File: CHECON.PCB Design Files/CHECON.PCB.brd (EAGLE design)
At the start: 81.7 x 51.7 mm, 48 parts

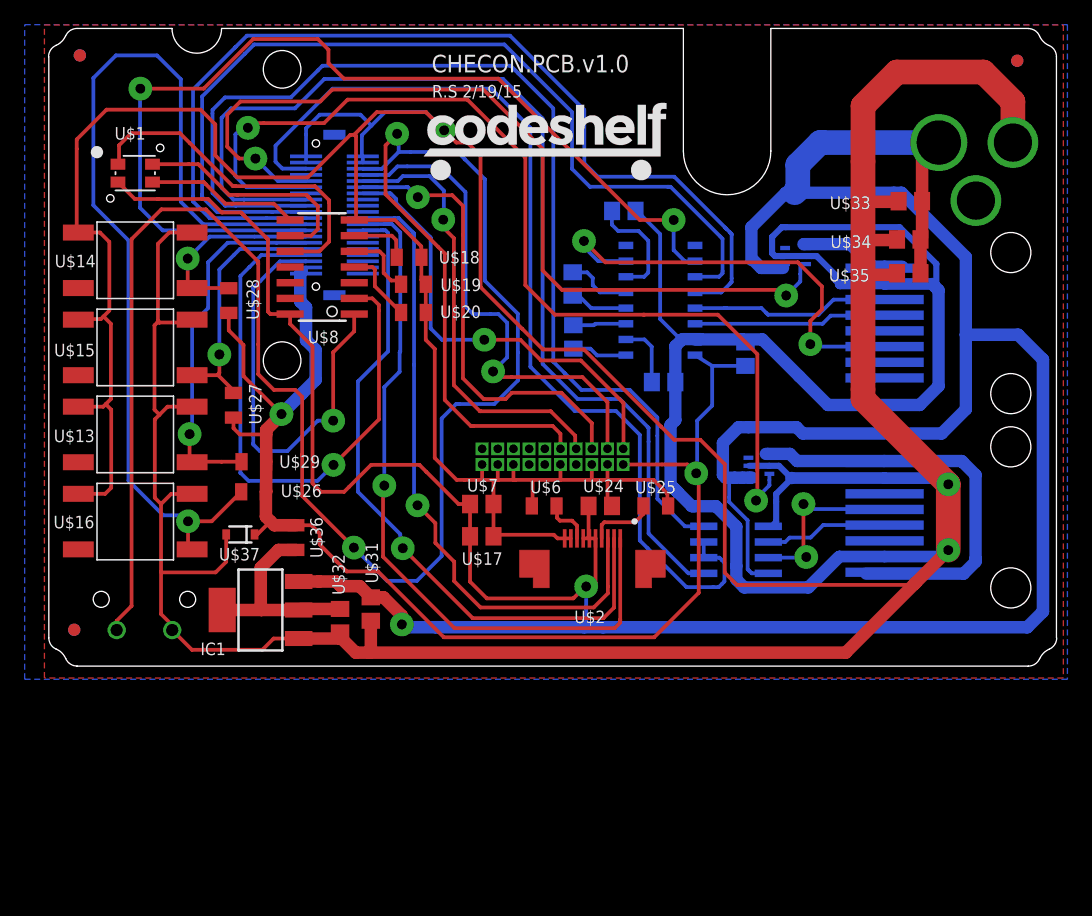
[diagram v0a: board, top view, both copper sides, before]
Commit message: CHECON.PCB.V1.0
Fixed some pin 1 markers, grounded unused input on 232, package names,
flipped FPC pins to correct pin 1 location
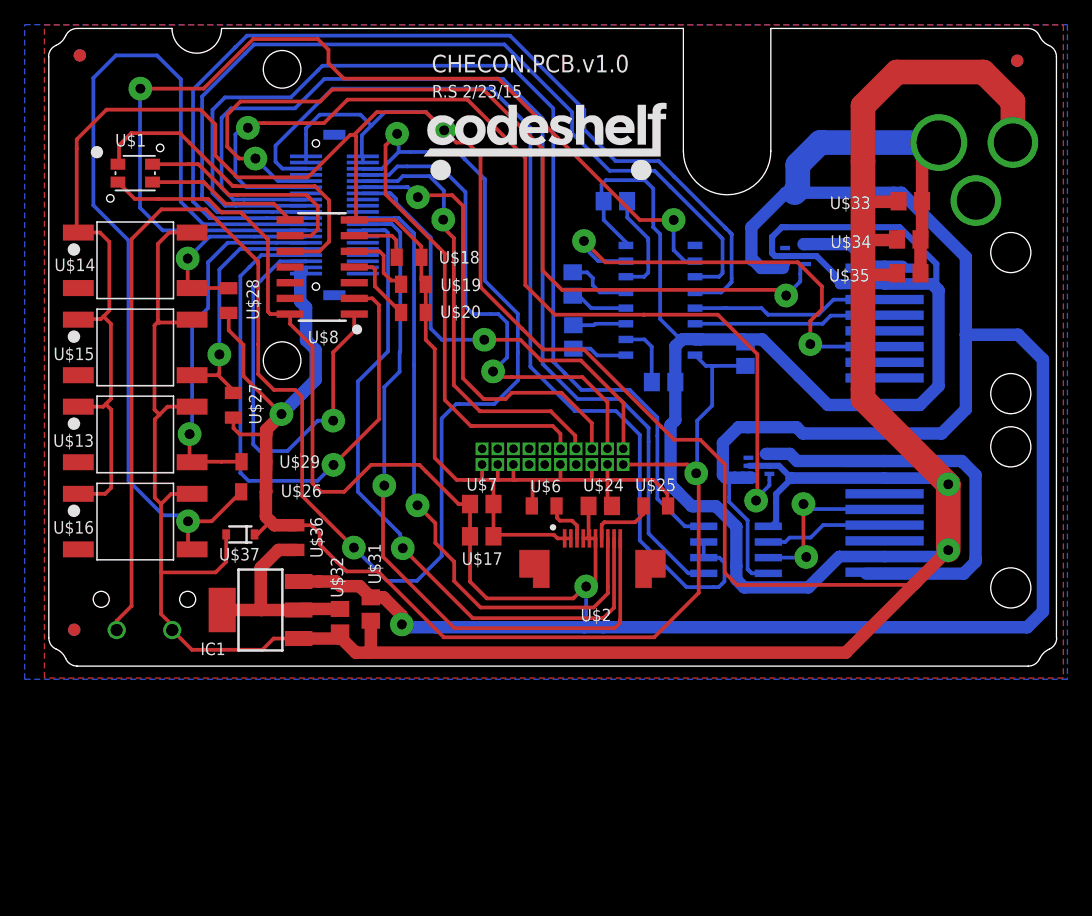
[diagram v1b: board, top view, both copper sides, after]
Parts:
- POSCON, SCANNER: device GW-devices:MOLEX-0955016649 -> GW-devices:RJ45_SMD
- U$1: device KW2:RGBLED -> KW2:PLCC4_SMALL
- U$2: device KW2:52745-1097 -> KW2:FPC
- moved U$23 1.04 mm to (5.08, 11.8), turned to 0 degrees
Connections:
- net GND: now also U$2.P$1, U$2.P$2, U2.8; no longer U$2.P$10, U$2.P$9
- net N$29: now also U$2.P$9; no longer U$2.P$2
- net N$30: now also U$2.P$10; no longer U$2.P$1
- net N$31: now also U$2.P$8; no longer U$2.P$3
- net N$32: now also U$2.P$3; no longer U$2.P$8
- net N$33: now also U$2.P$7; no longer U$2.P$4
- net V+: now also U$2.P$4; no longer U$2.P$7
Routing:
- net GND: track 566.0 -> 577.5 mm
- net N$26: track 75.3 -> 73.6 mm
- net N$10: track 80.8 -> 79.2 mm
- net N$41: track 81.0 -> 80.0 mm
- net N$22: track 9.14 -> 8.45 mm
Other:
- board text added: "R.S 2/23/15"
- board text removed: "R.S 2/19/15"

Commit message: Backlight Routing
Added backlight drivers and power monitoring. Mid-routing.
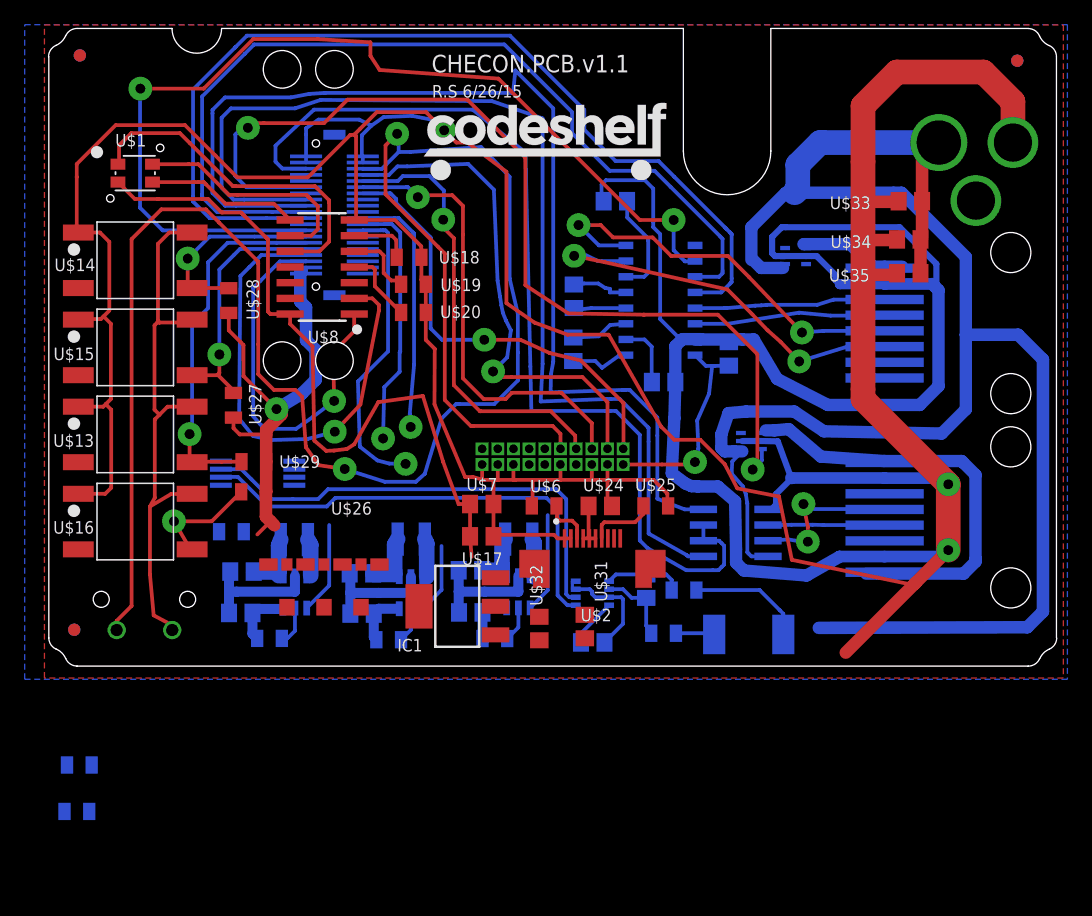
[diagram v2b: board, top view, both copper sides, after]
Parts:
- added C11, C14: 0.1uF, GW-devices:C0805
- added LQH3NPN100NM0L, U$47, U$49: 1212_IND, KW2:1212_IND
- added R10: (no value), GW-devices:R2512
- added R12, R13: 10, GW-devices:RF-C0805
- added U$44: SC4541, KW2:SOT23-6
- added U$45: PCA9632DP1, KW2:TSSOP-8
- added U$46: 10k, GW-devices:RF-C0805
- added U$50, U$51, U$52, U$53, U$54, U$55: 1uF, GW-devices:C0805
- added U$56: 6.6, GW-devices:RF-C0805
- added U$57, U$58: 3.3, GW-devices:RF-C0805
- added U$59: BL_CON, KW2:009155004301006
- added U$60, U$61: 4.7k, GW-devices:RF-C0805
- added U$62: INA219B, texas:DCN-R-PDSO-G8
- U$1: value (none) -> RGLBED; device KW2:PLCC4_SMALL -> KW2:RGBLED
- U$10: value (none) -> KW2_CPU_COMBO; device KW2:DF12_F -> KW2:BRAIN_COMBO
- U$2: value (none) -> 52745-1097; device KW2:FPC -> KW2:52745-1097
- U$3: value (none) -> 2X10JTAG
- U$30: value (none) -> RA_BUTTON
- U$36: value 0 -> SC4541; device GW-devices:RF-C0805 -> KW2:SOT23-6
- U$37: value (none) -> SC4541; device SparkFun:SOD-323 -> KW2:SOT23-6
- U$9: value (none) -> BARREL_CUI_PJ-002A
- moved U$36 18.6 mm to (-2.77, -19.8), flipped to the bottom, turned to 180 degrees
- moved U$31 17.4 mm to (2.61, -22.6)
- moved U$32 16.2 mm to (-1.08, -22.8)
- moved IC1 15.9 mm to (-7.73, -21.0)
- moved U$37 14.6 mm to (-11.5, -19.9), flipped to the bottom
- moved U$5 2.10 mm to (16.1, -7.59)
- moved U3 1.37 mm to (14.8, -15.0)
- moved U$21 1.35 mm to (14.3, -0.53)
- moved U$12 1.00 mm to (1.73, 4.13)
- moved U$11 1.00 mm to (1.68, -0.16)
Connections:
- removed net OUT1: IC1.2, IC1.4, U$32.2, U$36.1
- new net N$38: U$10.P$23, U2.9
- new net N$42: U$10.P$18, U$16.4, U$26.1
- new net N$43: U$36.4, U$37.4, U$44.4, U$45.1, U$46.2
- new net N$44: U$37.1, U$47.P$2, U$50.2
- new net N$45: U$10.P$7, U$45.7, U$61.2, U$62.6
- new net N$46: LQH3NPN100NM0L.P$2, U$36.1, U$52.2
- new net N$47: U$10.P$9, U$45.6, U$60.2, U$62.5
- new net N$48: U$44.1, U$49.P$2, U$51.2
- new net N$50: U$44.5, U$58.2
- new net N$51: U$44.6, U$55.1, U$58.1, U$59.P$3
- new net N$52: U$37.5, U$57.2
- new net N$53: U$37.6, U$54.1, U$57.1, U$59.P$2
- new net N$54: U$36.6, U$53.1, U$56.1, U$59.P$1
- new net N$55: U$36.5, U$56.2
- new net N$56: C11.1, R12.1, U$62.1
- new net N$57: C11.2, R13.1, U$62.2
- new net N$58: IC1.3, R10.2, R13.2, U$31.2
- net +3V3: now also C14.1, IC1.2, IC1.4, LQH3NPN100NM0L.P$1, U$32.2, U$36.3, U$37.3, U$44.3, U$45.8, U$47.P$1, U$49.P$1, U$60.1, U$61.1, U$62.4; no longer U$36.2, U$37.1
- net GND: now also C14.2, U$2.P$10, U$2.P$9, U$36.2, U$44.2, U$45.5, U$46.1, U$50.1, U$51.1, U$52.1, U$53.2, U$54.2, U$55.2, U$59.P$4, U$62.3, U$62.7, U$62.8; no longer U$2.P$1, U$2.P$2, U2.8
- net N$29: now also U$2.P$2; no longer U$2.P$9
- net N$30: now also U$2.P$1; no longer U$2.P$10
- net N$31: now also U$2.P$3; no longer U$2.P$8
- net N$32: now also U$2.P$8; no longer U$2.P$3
- net N$33: now also U$2.P$4; no longer U$2.P$7
- net N$34: now also SCANNER.P$5, U2.8; no longer U$10.P$23, U$16.4, U$26.1
- net N$40: now also U$10.P$16; no longer U$10.P$9
- net V+: now also R10.1, R12.2, U$2.P$7; no longer IC1.3, U$2.P$4, U$31.2
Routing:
- net N$40: track 72.4 -> 0.00 mm, vias 2 -> 0
- net V+: track 273.3 -> 219.8 mm, vias 2 -> 0
- net N$34: track 78.2 -> 33.0 mm, vias 1 -> 2
- net GND: track 577.5 -> 537.1 mm
- net N$30: track 58.8 -> 20.5 mm
- net +3V3: track 108.9 -> 70.7 mm
- net N$45: track 0.00 -> 38.2 mm
- net N$47: track 0.00 -> 37.8 mm
- net N$31: track 52.5 -> 20.4 mm
- net N$29: track 55.6 -> 24.6 mm
- net N$43: track 0.00 -> 21.3 mm
- net OUT1: track 16.4 -> 0.00 mm
- net N$6: track 167.0 -> 153.0 mm
- net N$42: track 0.00 -> 10.2 mm, vias 0 -> 1
- net N$16: track 47.1 -> 39.6 mm
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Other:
- board text added: "CHECON.PCB.v1.1"
- board text added: "R.S 6/26/15"
- board text removed: "CHECON.PCB.v1.0"
- board text removed: "R.S 2/23/15"

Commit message: Routing
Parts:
- moved IC1 23.5 mm to (15.4, -16.6), turned to 0 degrees
- moved U$31 16.2 mm to (18.8, -22.5), turned to 180 degrees
- moved U$32 14.4 mm to (13.3, -22.5), turned to 0 degrees
- moved U$20 1.81 mm to (-11.5, 1.02)
- moved U$19 1.71 mm to (-11.5, 3.41)
- moved U$18 1.14 mm to (-11.3, 6.19)
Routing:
- net N$45: track 38.2 -> 98.0 mm, vias 0 -> 2
- net N$47: track 37.8 -> 96.8 mm, vias 0 -> 2
- net +3V3: track 70.7 -> 127.0 mm
- net GND: track 537.1 -> 550.5 mm
- net N$42: track 10.2 -> 22.2 mm, vias 1 -> 2
- net N$40: track 0.00 -> 9.16 mm, vias 0 -> 1
- net N$2: track 37.4 -> 42.6 mm
- net V+: track 219.8 -> 222.9 mm
- net N$58: track 3.14 -> 6.00 mm
- net N$3: track 36.3 -> 38.9 mm
- net N$15: track 6.11 -> 7.48 mm
- net N$6: track 153.0 -> 154.1 mm
- net N$41: track 79.8 -> 80.9 mm
- net N$43: track 21.3 -> 22.4 mm
- net N$14: track 5.73 -> 6.33 mm

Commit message: Finished layout pending spring connector
Waiting for physical location of BL connector
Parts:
- U$56: value 6.6 -> 6.8
- U$62: device texas:DCN-R-PDSO-G8 -> KW2:DCN-R-PDSO-G8
- moved U$61 52.4 mm to (-38.1, 18.6), turned to 90 degrees
- moved U$60 52.0 mm to (-38.1, 14.4), turned to 270 degrees
- moved U$17 3.60 mm to (-2.14, -15.2)
- moved U$22 1.79 mm to (10.6, -3.62)
- moved U$23 1.66 mm to (3.58, 12.5)
- moved U$58 1.40 mm to (-21.5, -23.6)
- moved U$7 1.22 mm to (-4.54, -12.9)
- moved U$59 1.00 mm to (-19.5, -17.6)
- moved R10 0.66 mm to (15.7, -22.6), turned to 180 degrees
- moved U$6 0.40 mm to (-0.29, -12.9)
- moved C14 0.36 mm to (3.45, -24.2)
- moved U$46 0.32 mm to (-26.2, -14.7), turned to 180 degrees
- moved R12 0.30 mm to (10.6, -19.4)
- moved U$24 0.20 mm to (4.06, -12.9)
- moved U$57 0.10 mm to (-13.3, -23.6)
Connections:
- removed net N$58: IC1.3, R10.2, R13.2, U$31.2
- new net N$49: R10.1, R12.2, U$33.2, U$34.2, U$35.2, U$9.P$1
- net GND: now also U$2.P$1, U$2.P$2; no longer U$2.P$10, U$2.P$9
- net N$29: now also U$2.P$9; no longer U$2.P$2
- net N$30: now also U$2.P$10; no longer U$2.P$1
- net N$31: now also U$2.P$8; no longer U$2.P$3
- net N$32: now also U$2.P$3; no longer U$2.P$8
- net N$33: now also U$2.P$7; no longer U$2.P$4
- net V+: now also IC1.3, R10.2, R13.2, U$2.P$4, U$31.2; no longer R10.1, R12.2, U$2.P$7, U$33.2, U$34.2, U$35.2, U$9.P$1
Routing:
- net N$42: track 22.2 -> 112.1 mm, vias 2 -> 3
- net +3V3: track 127.0 -> 216.7 mm, vias 2 -> 6
- net N$40: track 9.16 -> 90.2 mm, vias 1 -> 2
- net N$38: track 0.00 -> 71.9 mm, vias 0 -> 2
- net N$49: track 0.00 -> 67.0 mm, vias 0 -> 1
- net N$43: track 22.4 -> 60.6 mm, vias 0 -> 2
- net N$30: track 20.5 -> 55.2 mm
- net V+: track 222.9 -> 252.5 mm, vias 0 -> 4
- net N$31: track 20.4 -> 49.2 mm
- net N$29: track 24.6 -> 52.0 mm
- net N$54: track 4.61 -> 16.6 mm, vias 0 -> 1
- net N$51: track 5.46 -> 17.1 mm, vias 0 -> 1
- net N$53: track 4.43 -> 13.6 mm, vias 0 -> 1
- net N$58: track 6.00 -> 0.00 mm
- net GND: track 550.5 -> 555.1 mm, vias 3 -> 6
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- removed copper zone on layer 1, net GND
- removed copper zone on layer 16, net GND
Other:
- board size 81.7 x 51.7 mm -> 81.7 x 51.6 mm
- board text added: "R.S 7/6/15"
- board text removed: "R.S 6/26/15"

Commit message: v1.1P1
Submitted to Chris. Forgot bus terminator
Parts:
- moved U$59 0.60 mm to (-19.5, -18.2)
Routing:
- net +3V3: track 216.7 -> 218.0 mm
- net N$51: track 17.1 -> 16.4 mm
- net GND: track 555.1 -> 554.5 mm
- net N$53: track 13.6 -> 13.0 mm
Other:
- board text added: "CHECON.PCB.v1.1P1"
- board text added: "R.S 7/8/15"
- board text removed: "CHECON.PCB.v1.1"
- board text removed: "R.S 7/6/15"

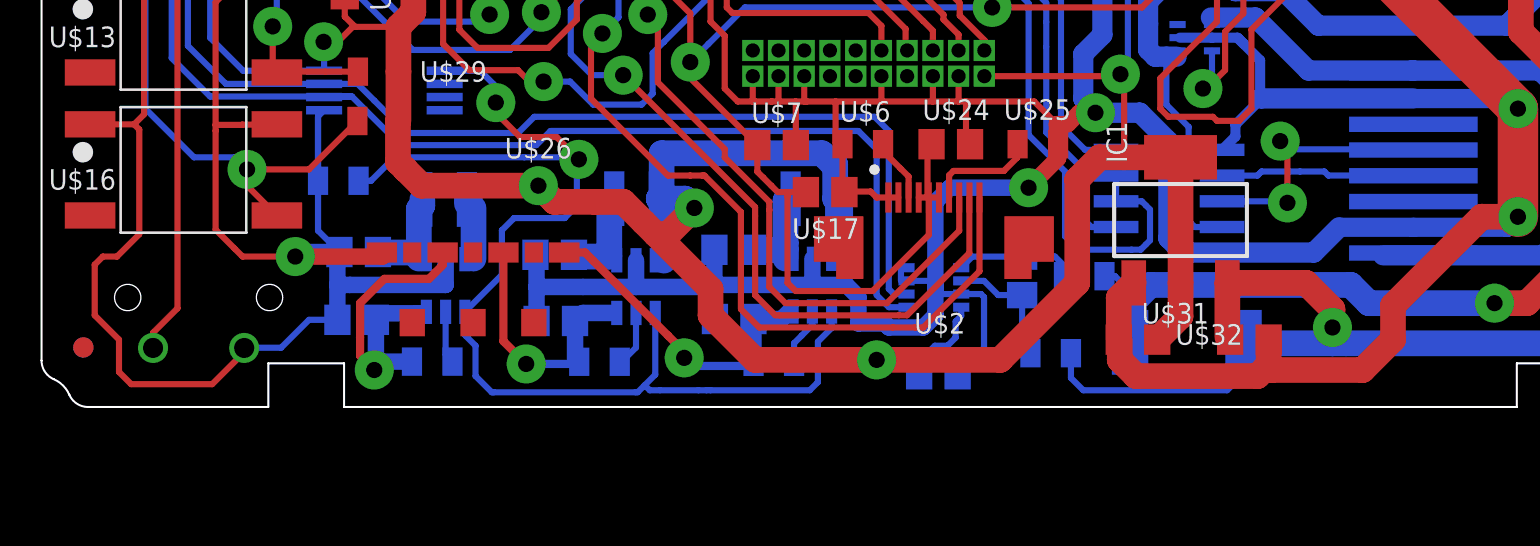
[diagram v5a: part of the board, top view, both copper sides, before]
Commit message: Added bus terminator to schematic
Still need to add to layout
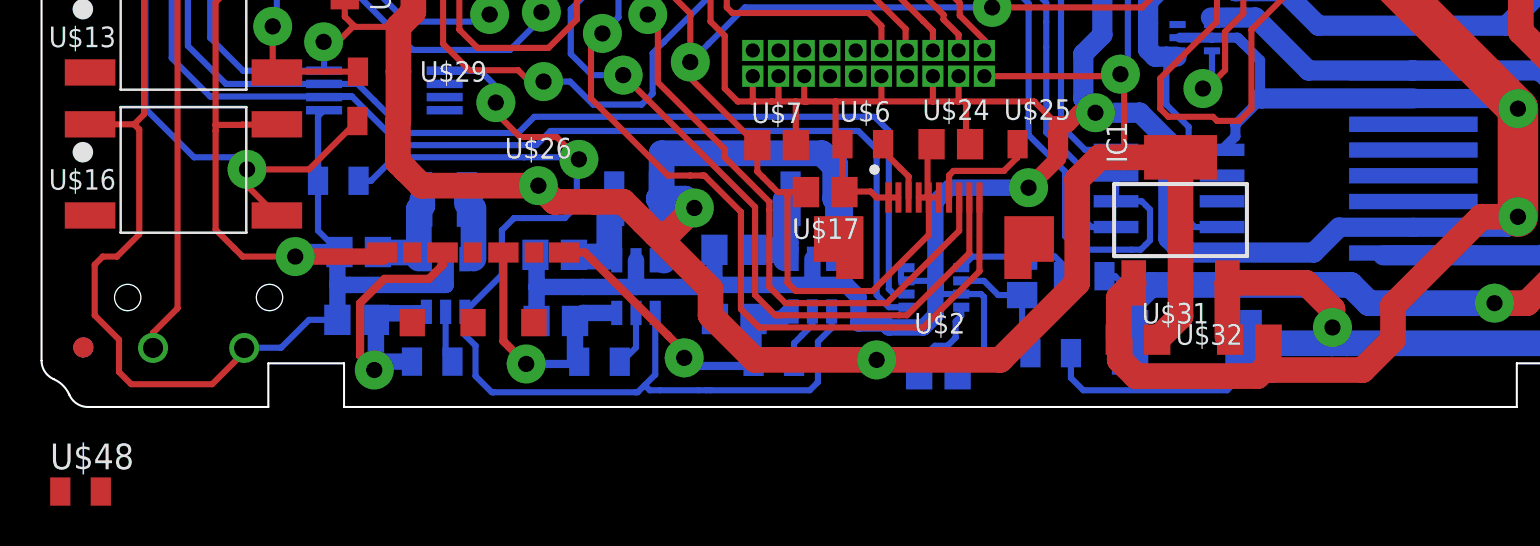
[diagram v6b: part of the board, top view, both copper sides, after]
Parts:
- added U$48: 120, GW-devices:RF-C0805
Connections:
- net N$19: now also U$48.1
- net N$20: now also U$48.2
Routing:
- net N$19: track 13.2 -> 0.00 mm, vias 2 -> 0
- net N$20: track 9.88 -> 0.00 mm
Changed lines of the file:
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@@
 <element name="C11" library="GW-devices" package="C0805" value="0.1uF" x="7.5814" y="-19.3528" rot="MR270"/>
 <element name="C14" library="GW-devices" package="C0805" value="0.1uF" x="3.4472" y="-24.2096" rot="MR180"/>
+<element name="U$48" library="GW-devices" package="RF-C0805" value="120" x="-38.9" y="-30">
+<attribute name="MFGN" value="Panasonic" x="-38.9" y="-30" size="1.778" layer="27" display="off"/>
+<attribute name="MFGP" value="ERJ-6ENF4701V" x="-38.9" y="-30" size="1.778" layer="27" display="off"/>
+</element>
 </elements>
 <signals>
@@
 <wire x1="-4" y1="-15.44468125" x2="-4" y2="-15.2162" width="0.3048" layer="1"/>
 </signal>
-<signal name="N$19">
-<contactref element="U3" pad="7"/>
-<contactref element="POSCON" pad="P$4"/>
-<wire x1="26.8614" y1="-13.1064" x2="26.895" y2="-13.14" width="0.3048" layer="16"/>
-<via x="20.6756" y="-15.748" extent="1-16" drill="0.8" diameter="1.9304"/>
-<via x="20.32" y="-12.7" extent="1-16" drill="0.8" diameter="1.9304"/>
-<wire x1="26.8778" y1="-13.1572" x2="26.895" y2="-13.14" width="0.3048" layer="16"/>
-<wire x1="26.8614" y1="-13.1064" x2="20.7264" y2="-13.1064" width="0.3048" layer="16"/>
-<wire x1="20.7264" y1="-13.1064" x2="20.32" y2="-12.7" width="0.3048" layer="16"/>
-<wire x1="17.4498" y1="-15.6718" x2="20.5994" y2="-15.6718" width="0.3048" layer="16"/>
-<wire x1="20.5994" y1="-15.6718" x2="20.6756" y2="-15.748" width="0.3048" layer="16"/>
-<wire x1="20.32" y1="-12.7" x2="20.6756" y2="-13.0556" width="0.3048" layer="1"/>
-<wire x1="20.6756" y1="-13.0556" x2="20.6756" y2="-15.748" width="0.3048" layer="1"/>
-</signal>
-<signal name="N$20">
-<contactref element="U3" pad="6"/>
-<contactref element="POSCON" pad="P$5"/>
-<wire x1="26.6954" y1="-14.4018" x2="26.7716" y2="-14.478" width="0.3048" layer="16"/>
-<wire x1="26.7716" y1="-14.478" x2="26.827" y2="-14.478" width="0.3048" layer="16"/>
-<wire x1="26.827" y1="-14.478" x2="26.895" y2="-14.41" width="0.3048" layer="16"/>
-<wire x1="17.4498" y1="-14.4018" x2="19.1982" y2="-14.4018" width="0.3048" layer="16"/>
-<wire x1="19.1982" y1="-14.4018" x2="19.3" y2="-14.3" width="0.3048" layer="16"/>
-<wire x1="19.3" y1="-14.3" x2="19.4" y2="-14.2" width="0.3048" layer="16"/>
-<wire x1="19.4" y1="-14.2" x2="21.3" y2="-14.2" width="0.3048" layer="16"/>
-<wire x1="21.3" y1="-14.2" x2="22.5" y2="-14.2" width="0.3048" layer="16"/>
-<wire x1="22.5" y1="-14.2" x2="22.7" y2="-14.4" width="0.3048" layer="16"/>
-<wire x1="22.7" y1="-14.4" x2="26.885" y2="-14.4" width="0.3048" layer="16"/>
-<wire x1="26.885" y1="-14.4" x2="26.895" y2="-14.41" width="0.5" layer="16"/>
-</signal>
 <signal name="N$16">
 <contactref element="U$8" pad="2"/>
@@
 <wire x1="32.2" y1="3.5988" x2="29.8044" y2="5.9944" width="1.27" layer="1"/>
 </signal>
+<signal name="N$19">
+<contactref element="U3" pad="7"/>
+<contactref element="U$48" pad="1"/>
+<contactref element="POSCON" pad="P$4"/>
+<wire x1="17.4498" y1="-15.6718" x2="-39.9" y2="-30" width="0" layer="19" extent="1-16"/>
+<wire x1="26.895" y1="-13.14" x2="17.4498" y2="-15.6718" width="0" layer="19" extent="16-16"/>
+</signal>
+<signal name="N$20">
+<contactref element="U3" pad="6"/>
+<contactref element="U$48" pad="2"/>
+<contactref element="POSCON" pad="P$5"/>
+<wire x1="17.4498" y1="-14.4018" x2="-37.9" y2="-30" width="0" layer="19" extent="1-16"/>
+<wire x1="26.895" y1="-14.41" x2="17.4498" y2="-14.4018" width="0" layer="19" extent="16-16"/>
+</signal>
 </signals>

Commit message: Through-hole switch?
Replaced buttons with though-hole versions (I think)
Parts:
- U$13, U$14, U$15, U$16: value (none) -> SWITCH-TACTILE-FSM; device GW-devices:ESWITCH-TL3301PF -> GW-devices:SWITCH-TACTILE-FSM
- moved U$48 61.5 mm to (20.7, -14.9), flipped to the bottom, turned to 90 degrees
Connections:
- net GND: now also U$13.P$1, U$13.P$2, U$14.P$1, U$14.P$2, U$15.P$1, U$15.P$2, U$16.P$1, U$16.P$2; no longer U$13.1, U$13.2, U$14.1, U$14.2, U$15.1, U$15.2, U$16.1, U$16.2
- net N$35: now also U$15.P$4; no longer U$15.4
- net N$36: now also U$14.P$4; no longer U$14.4
- net N$37: now also U$13.P$4; no longer U$13.4
- net N$42: now also U$16.P$4; no longer U$16.4
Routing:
- net N$19: track 0.00 -> 11.7 mm
- net N$20: track 0.00 -> 6.25 mm, vias 0 -> 1
